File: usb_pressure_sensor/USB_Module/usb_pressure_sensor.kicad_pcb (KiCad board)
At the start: 2 copper layers, 45 x 26 mm, 25 parts, among them IC1 STM32F042F6P6, IC2 MCP1700, J1 CONN_02x09, J2 MODULE_BRIDGE, P1 SWD_TC, U1 MICRO_USB, U2 SN74LVC1GX04, U3 KSC341J:SWITCH, Y1 Crystal 32.768kHz

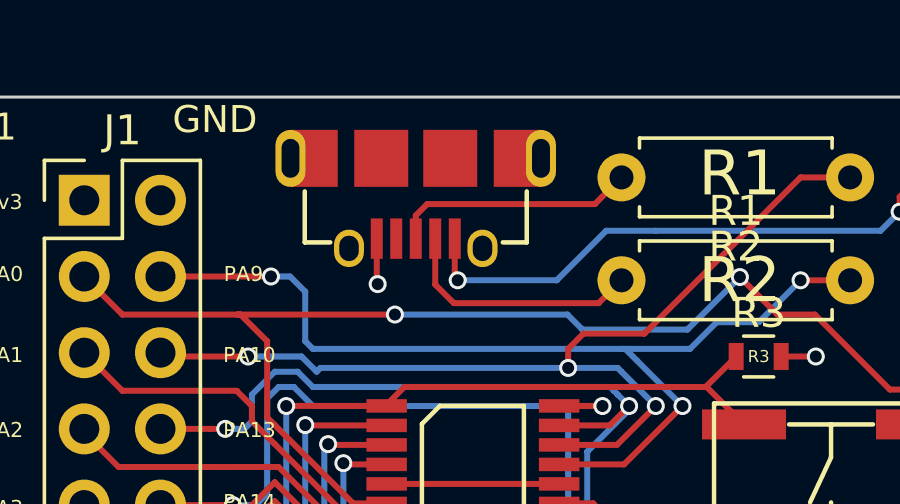
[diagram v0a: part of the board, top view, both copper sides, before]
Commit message: Moved usb connector
The connector has a line on the footprint which corresponds to the edge of the pcb so I moved it upwards such that this line becomes coincident with the pcb cut edge
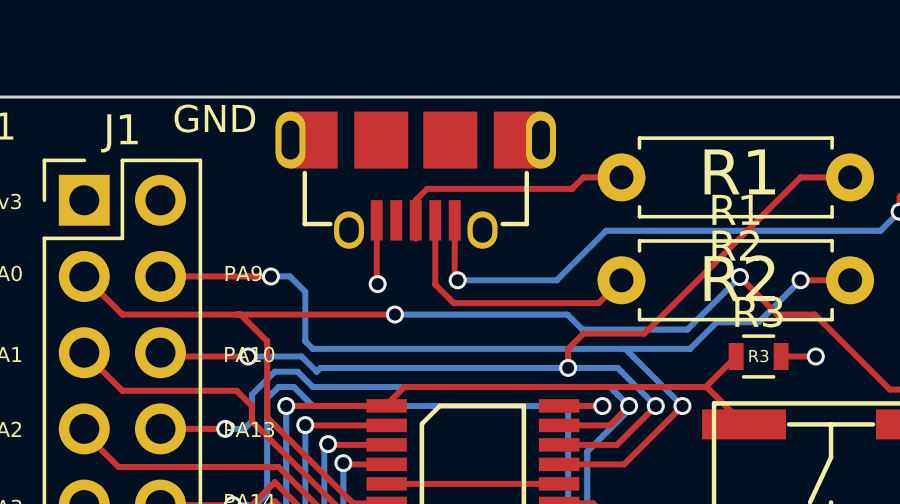
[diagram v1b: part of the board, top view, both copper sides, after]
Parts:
- moved U1 0.61 mm to (131.4, 97.4)
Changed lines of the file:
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@@
-(kicad_pcb (version 4) (host pcbnew 4.0.6)
+(kicad_pcb (version 4) (host pcbnew 4.0.6-e0-6349~53~ubuntu16.04.1)
   (general
     (links 63)
-    (no_connects 0)
+    (no_connects 1)
     (area 116.704095 93.319 167.557143 123.275)
     (thickness 1.6)
     (drawings 37)
-    (tracks 386)
+    (tracks 388)
     (zones 0)
     (modules 25)
@@
   (page A4)
   (layers
-    (0 F.Cu signal hide)
-    (31 B.Cu signal hide)
+    (0 F.Cu signal)
+    (31 B.Cu signal)
     (32 B.Adhes user hide)
     (33 F.Adhes user hide)
@@
     (last_trace_width 0.2)
     (trace_clearance 0.2)
-    (zone_clearance 0.254)
+    (zone_clearance 0.508)
     (zone_45_only no)
     (trace_min 0.2)
@@
   )
   (module agg:MICROUSB_MOLEX_47589-0001 (layer F.Cu)
-    (at 131.445 98.044 180)
+    (at 131.445 97.4344 180)
     (fp_text reference U1 (at 0 -4.75 180) (layer F.Fab)
       (effects (font (size 1 1) (thickness 0.15)))
@@
   (segment (start 132.715 102.87) (end 137.541 102.87) (width 0.2) (layer F.Cu) (net 25))
   (segment (start 132.095 102.25) (end 132.715 102.87) (width 0.2) (layer F.Cu) (net 25))
+  (segment (start 138.303 98.679) (end 137.033 98.679) (width 0.2) (layer F.Cu) (net 26) (status 400000))
+  (segment (start 131.826 99.06) (end 131.445 99.441) (width 0.2) (layer F.Cu) (net 26) (status 800000))
+  (segment (start 136.652 99.06) (end 131.826 99.06) (width 0.2) (layer F.Cu) (net 26))
+  (segment (start 137.033 98.679) (end 136.652 99.06) (width 0.2) (layer F.Cu) (net 26))
+  (segment (start 131.445 99.441) (end 131.445 100.1094) (width 0.2) (layer F.Cu) (net 26) (status C00000))
   (segment (start 131.445 100.719) (end 131.445 99.949) (width 0.2) (layer F.Cu) (net 26))
-  (segment (start 137.414 99.568) (end 138.303 98.679) (width 0.2) (layer F.Cu) (net 26))
-  (segment (start 131.826 99.568) (end 137.414 99.568) (width 0.2) (layer F.Cu) (net 26))
-  (segment (start 131.445 99.949) (end 131.826 99.568) (width 0.2) (layer F.Cu) (net 26))
   (segment (start 154.5 108.4) (end 154.5 106.25) (width 0.2) (layer F.Cu) (net 31))
   (segment (start 152 108.4) (end 152 106.75) (width 0.2) (layer F.Cu) (net 32))
